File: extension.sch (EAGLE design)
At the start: 219 parts, among them IC1001 AQV252G2S, IC1002 AQV252G2S, IC1003 AQV252G2S, IC1101 UA78L05ACPK, IC1102 ADUM3300ARW, IC1301 UA78L05ACPK, IC1302 LTC485CS8#PBF, IC1303 ADUM3401ARW, IC1701 ADR3425ARJZ, IC1901 UA78L05ACPK, IC1902 ADUM3402ARW, IC1903 ADUM3402ARW, IC2001 AQV25G2S, IC2002 AQV25G2S, IC2003 AQV25G2S, IC2004 AQV25G2S, IC2005 AQV25G2S, IC2006 AQV25G2S, IC801 KA7805ERTF, IC802 CPC1008N, IC803 TJA1052IT/1Y, T1001 IRLML0100TRPBF, T1002 IRLML0100TRPBF, T1003 IRLML0100TRPBF, T1501 BSS84P, T2001 IRLML0100TRPBF, T2002 IRLML0100TRPBF, T2003 IRLML0100TRPBF, T2004 IRLML0100TRPBF, T2005 IRLML0100TRPBF, T2006 IRLML0100TRPBF, T801 IRLML0100TRPBF, T901 BUK964R8-60E, X1201 43045-0400_MOLEX_4PIN, X1202 43045-0400_MOLEX_4PIN, X1203 43045-0400_MOLEX_4PIN, X1301 43045-0600_MOLEX_6PIN, X1701 43045-1200_MOLEX_12PIN, X1901 43045-1000_MOLEX_10PIN, X2001 43045-1200_MOLEX_12PIN, X801 43045-0400_MOLEX_4PIN

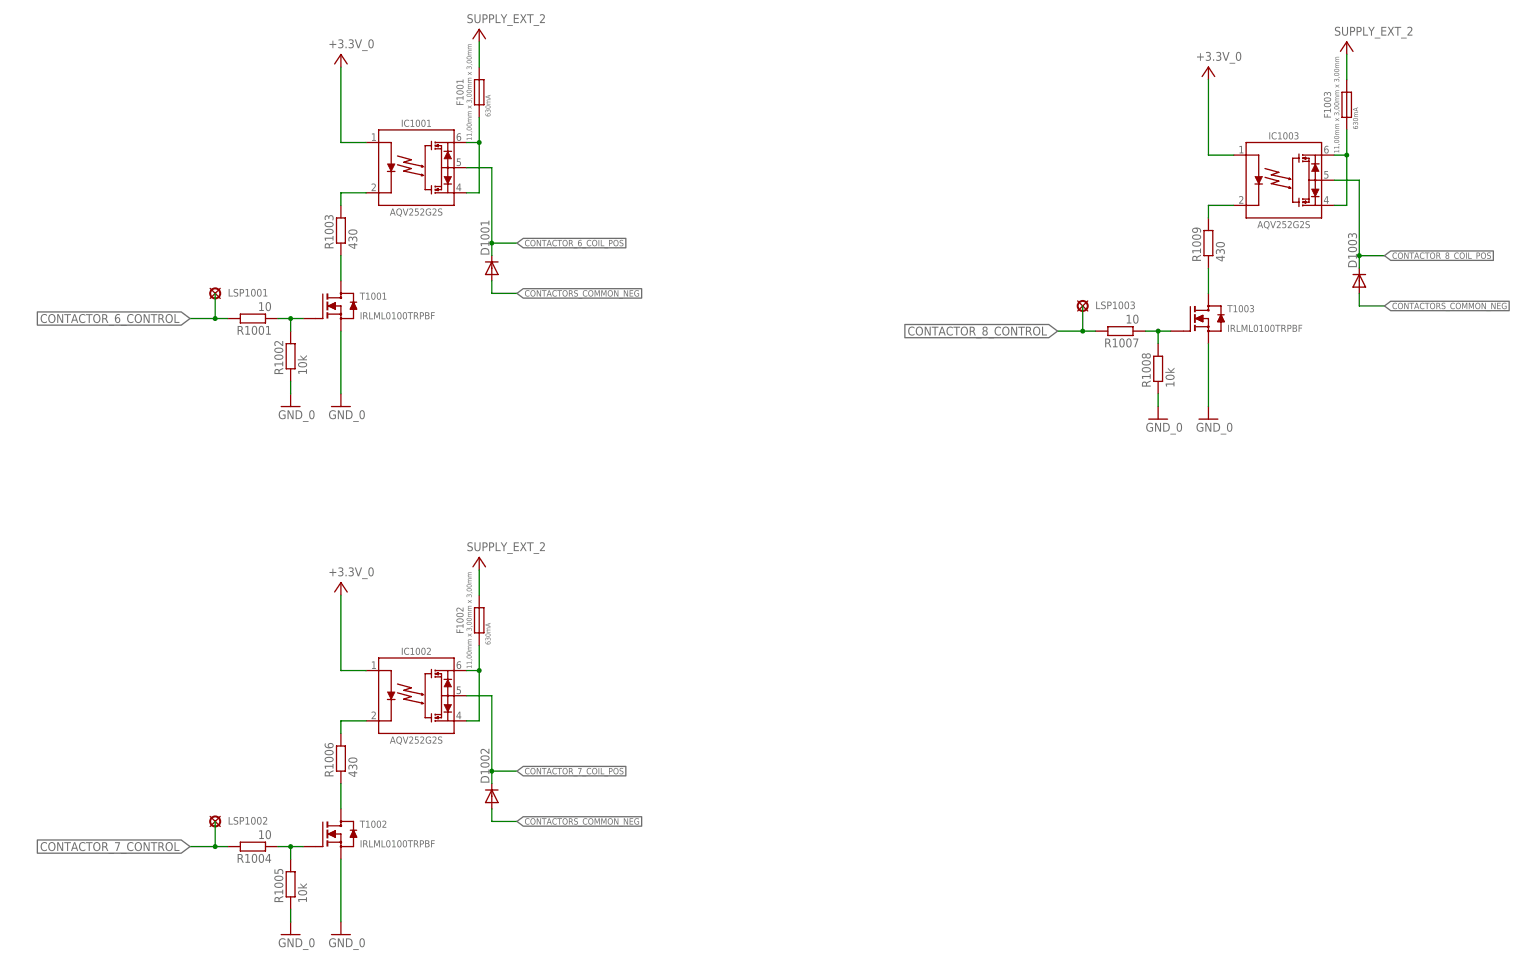
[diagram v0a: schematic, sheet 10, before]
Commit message: fixed fuse value in schematic
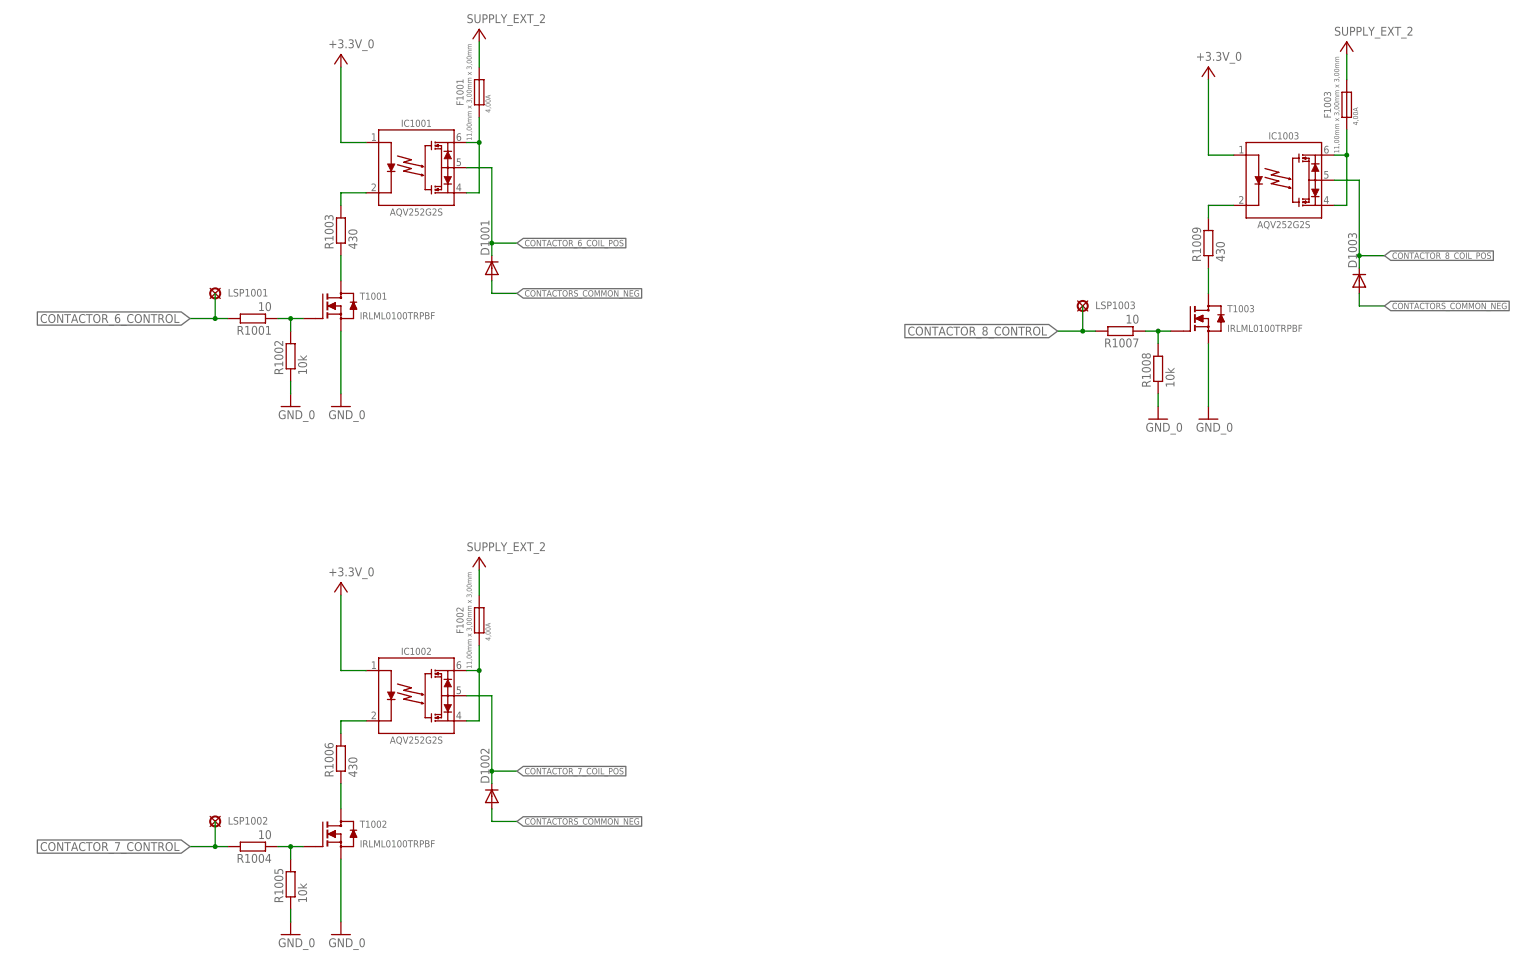
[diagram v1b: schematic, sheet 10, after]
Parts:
- F1001, F1002, F1003: value 630MA_UMT -> 4,00A_UMT; device 0_LES_SICHERUNG.SMD:630MA_UMT -> 0_LES_SICHERUNG.SMD:4,00A_UMT
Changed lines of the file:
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@@
 <setting verticaltext="up"/>
 </settings>
-<grid distance="0.1" unitdist="inch" unit="inch" style="lines" multiple="1" display="no" altdistance="0.01" altunitdist="inch" altunit="inch"/>
+<grid distance="100" unitdist="mil" unit="mil" style="lines" multiple="1" display="yes" altdistance="10" altunitdist="mil" altunit="mil"/>
 <layers>
 <layer number="1" name="Top" color="4" fill="1" visible="yes" active="no"/>
@@
 <part name="GND_EXT_7" library="foxBMS_BMS-Master_V1.00_A" deviceset="GND_EXT_2" device=""/>
 <part name="GND_EXT_13" library="foxBMS_BMS-Master_V1.00_A" deviceset="GND_EXT_2" device=""/>
-<part name="F1001" library="0_LES_SICHERUNG.SMD" deviceset="*_UMT" device="" technology="630MA"/>
-<part name="F1002" library="0_LES_SICHERUNG.SMD" deviceset="*_UMT" device="" technology="630MA"/>
-<part name="F1003" library="0_LES_SICHERUNG.SMD" deviceset="*_UMT" device="" technology="630MA"/>
+<part name="F1001" library="0_LES_SICHERUNG.SMD" deviceset="*_UMT" device="" technology="4,00A" value="4,00A_UMT"/>
+<part name="F1002" library="0_LES_SICHERUNG.SMD" deviceset="*_UMT" device="" technology="4,00A" value="4,00A_UMT"/>
+<part name="F1003" library="0_LES_SICHERUNG.SMD" deviceset="*_UMT" device="" technology="4,00A" value="4,00A_UMT"/>
 <part name="R1101" library="custom_passiv" deviceset="R*" device="0603" technology="_MET_" value="47"/>
 <part name="R1102" library="custom_passiv" deviceset="R*" device="0603" technology="_MET_" value="47"/>
